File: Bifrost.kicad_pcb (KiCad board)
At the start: 4 copper layers, 68.6 x 53.3 mm, 59 parts, among them J1 OIP, U1 AD5932, U2 BGA2851, U3 AD8000, U4 BGA2851, U5 AD5932, X1 SPXO-50M

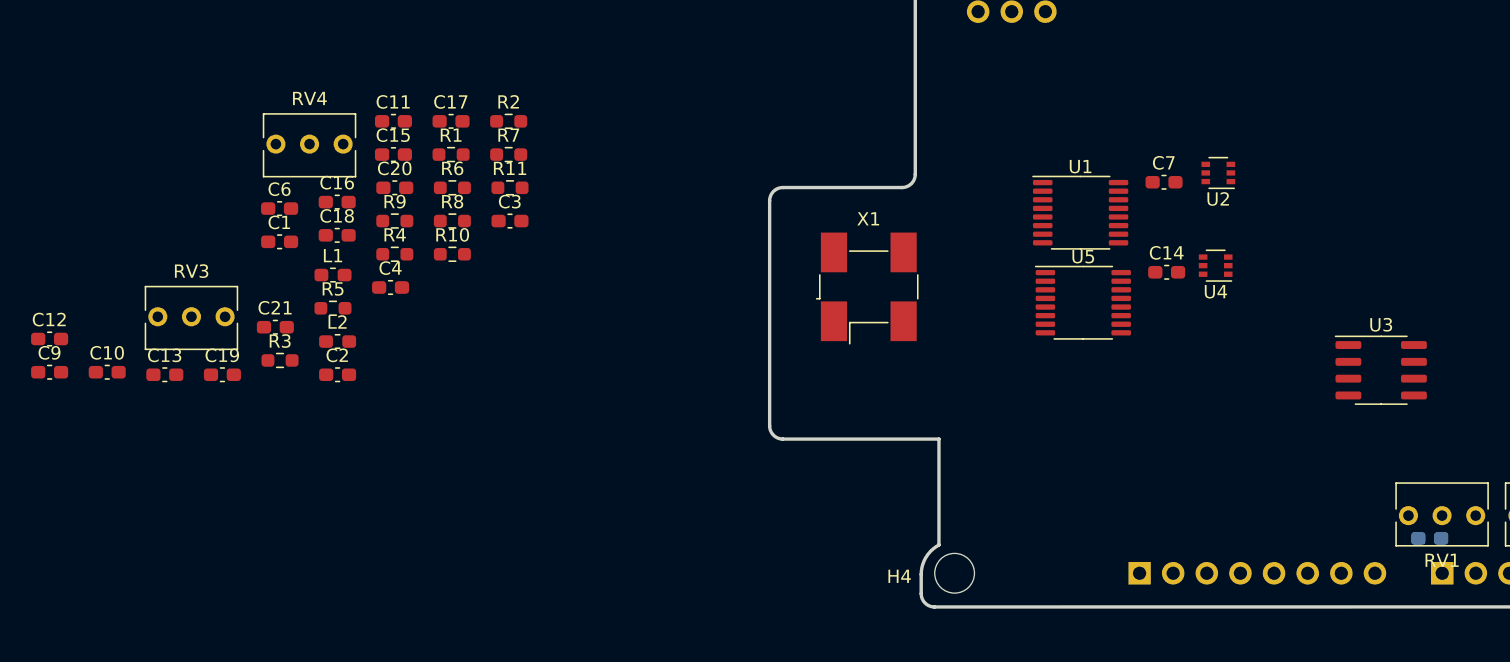
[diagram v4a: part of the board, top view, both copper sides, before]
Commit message: Progressed in placement
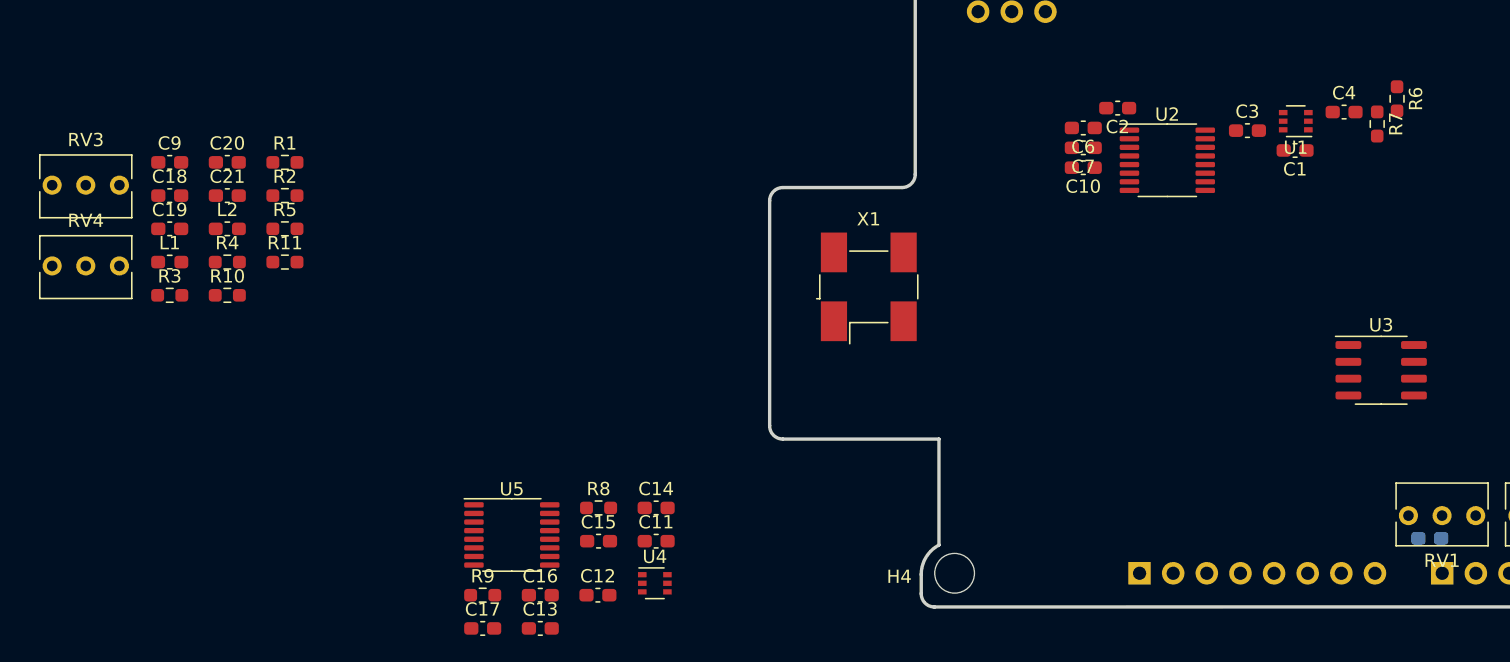
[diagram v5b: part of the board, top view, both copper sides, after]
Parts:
- C1: value 10n -> 100n
- C10, C15, C7: value 53n -> 100n
- C12, C2: value 100n -> 10n
- C13: value 10n -> 53n
- C3, C4: value 100n -> 53n
- U1: value AD5932 -> BGA2851; footprint Package_SO:TSSOP-16_4.4x5mm_P0.65mm -> Package_TO_SOT_SMD:SOT-363_SC-70-6
- U2: value BGA2851 -> AD5932; footprint Package_TO_SOT_SMD:SOT-363_SC-70-6 -> Package_SO:TSSOP-16_4.4x5mm_P0.65mm
- moved C1 77.0 mm to (153.9, 97.2), turned to 180 degrees
- moved C10 75.3 mm to (137.9, 98.5), turned to 180 degrees
- moved C4 73.2 mm to (157.6, 94.3)
- moved R6 71.7 mm to (161.6, 93.3), turned to 270 degrees
- moved R7 65.6 mm to (160.1, 95.2), turned to 270 degrees
- moved C2 62.3 mm to (140.5, 94.0), turned to 180 degrees
- moved C6 61.0 mm to (137.9, 95.5), turned to 180 degrees
- moved C3 56.1 mm to (150.3, 95.7)
- moved U4 48.7 mm to (105.5, 129.9), turned to 0 degrees
- moved U5 46.6 mm to (94.7, 126.2)
- moved C12 45.7 mm to (101.2, 130.8)
- moved C14 42.5 mm to (105.6, 124.2)
- moved C17 38.4 mm to (92.5, 133.3)
- moved C11 37.4 mm to (105.6, 126.7)
- moved C13 34.2 mm to (96.9, 133.3)
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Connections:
- AD1 pad 2: (no net) -> /AD1
- AD1 pad 3: (no net) -> /AD2
- AD1 pad 5: (no net) -> /AD4
- AD1 pad 6: (no net) -> /AD5
- C1 pad 1: Net-(C1-Pad1) -> VDDA
- C1 pad 2: VDDA -> GND
- C10 pad 2: Net-(C10-Pad2) -> GND
- C12 pad 1: VDDA -> Net-(C12-Pad1)
- C12 pad 2: GND -> VDDA
- C13 pad 2: VDDA -> Net-(C13-Pad2)
- C14 pad 2: Net-(C14-Pad2) -> /sheet61E7139B/Fout
- C15 pad 1: Net-(C15-Pad1) -> VDDA
- C15 pad 2: Net-(C15-Pad2) -> GND
- C16 pad 1: Net-(C16-Pad1) -> VDD
- C17 pad 1: VDD -> Net-(C17-Pad1)
- C2 pad 1: VDDA -> Net-(C2-Pad1)
- C2 pad 2: GND -> VDDA
- C3 pad 1: VDD -> Net-(C3-Pad1)
- C3 pad 2: GND -> Net-(C3-Pad2)
- C4 pad 2: GND -> /Sheet61C59086/Fout
- C7 pad 1: Net-(C7-Pad1) -> VDD
- C7 pad 2: Net-(C7-Pad2) -> GND
- ICSP1 pad 1: (no net) -> /MISO2
- ICSP1 pad 2: (no net) -> /+5V_Adr_3
- ICSP1 pad 3: (no net) -> /SCK2
- ICSP1 pad 4: (no net) -> /MOSI2
- ICSP1 pad 5: (no net) -> /RESET2
- ICSP2 pad 1: (no net) -> /MISO_0
- ICSP2 pad 3: (no net) -> /SCK_0
- ICSP2 pad 4: (no net) -> /MOSI_0
- ICSP2 pad 5: (no net) -> /RESET_0
- IOH1 pad 1: (no net) -> /IO8
- IOH1 pad 10: (no net) -> /SCL
- IOH1 pad 2: (no net) -> /IO9
- IOH1 pad 3: /SEN -> /SS
- IOH1 pad 8: (no net) -> /AREF
- IOH1 pad 9: (no net) -> /SDA
- IOL1 pad 1: (no net) -> /IO0
- IOL1 pad 2: (no net) -> /IO1
- POWER1 pad 1: (no net) -> Net-(POWER1-Pad1)
- POWER1 pad 3: (no net) -> /RESET
- POWER1 pad 4: (no net) -> /+3V3
- POWER1 pad 5: (no net) -> /+5V_Ard_1
- POWER1 pad 8: (no net) -> /VIN
- R2 pad 2: Net-(C10-Pad2) -> /Sheet61C59086/Fout
- R3 pad 2: Net-(C15-Pad2) -> /sheet61E7139B/Fout
- R49 pad 1: /SCK_S -> /SCK
- R52 pad 1: /SDI_S -> /MOSI
- R52 pad 2: /MOSI -> /SDI
- R53 pad 1: (no net) -> /IO9
- R53 pad 2: /MISO -> /SEN2
- R56 pad 1: /SEN_S -> /SS
- R6 pad 2: Net-(C10-Pad2) -> /Sheet61C59086/Fout
- R7 pad 1: Net-(C10-Pad2) -> /Sheet61C59086/Fout
- R8 pad 2: Net-(C15-Pad2) -> /sheet61E7139B/Fout
- R9 pad 1: Net-(C15-Pad2) -> /sheet61E7139B/Fout
- U1 pad 1: Net-(C1-Pad1) -> VDDA
- U1 pad 2: VDDA -> GND
- U1 pad 3: VDD -> Net-(C4-Pad1)
- U1 pad 4: Net-(C4-Pad1) -> GND
- U1 pad 6: Net-(U1-Pad6) -> Net-(C3-Pad2)
- U2 pad 1: VDDA -> Net-(C2-Pad1)
- U2 pad 2: GND -> VDDA
- U2 pad 3: Net-(C10-Pad1) -> VDD
- U2 pad 4: GND -> Net-(C10-Pad1)
- U2 pad 6: Net-(C7-Pad2) -> /Sheet61C59086/MCLK
- U3 pad 1: (no net) -> Net-(U3-Pad1)
- U3 pad 5: (no net) -> Net-(U3-Pad5)
- U3 pad 8: (no net) -> Net-(U3-Pad8)
- U4 pad 3: Net-(C15-Pad1) -> Net-(C14-Pad1)
- U4 pad 6: Net-(C14-Pad2) -> Net-(C13-Pad2)
- U5 pad 1: Net-(C13-Pad1) -> Net-(C12-Pad1)
- U5 pad 11: /SDI_S -> /SDI
- U5 pad 12: /SCK_S -> /SCK
- U5 pad 13: /SEN_S -> /SEN2
- U5 pad 16: Net-(C14-Pad1) -> Net-(C13-Pad1)
- U5 pad 4: Net-(C16-Pad1) -> Net-(C17-Pad1)
- U5 pad 6: Net-(U1-Pad6) -> /Sheet61C59086/MCLK
- U5 pad 7: (no net) -> Net-(U5-Pad7)
- U5 pad 8: (no net) -> Net-(U5-Pad8)
- X1 pad 1: (no net) -> Net-(X1-Pad1)
- X1 pad 3: Net-(U1-Pad6) -> /Sheet61C59086/MCLK

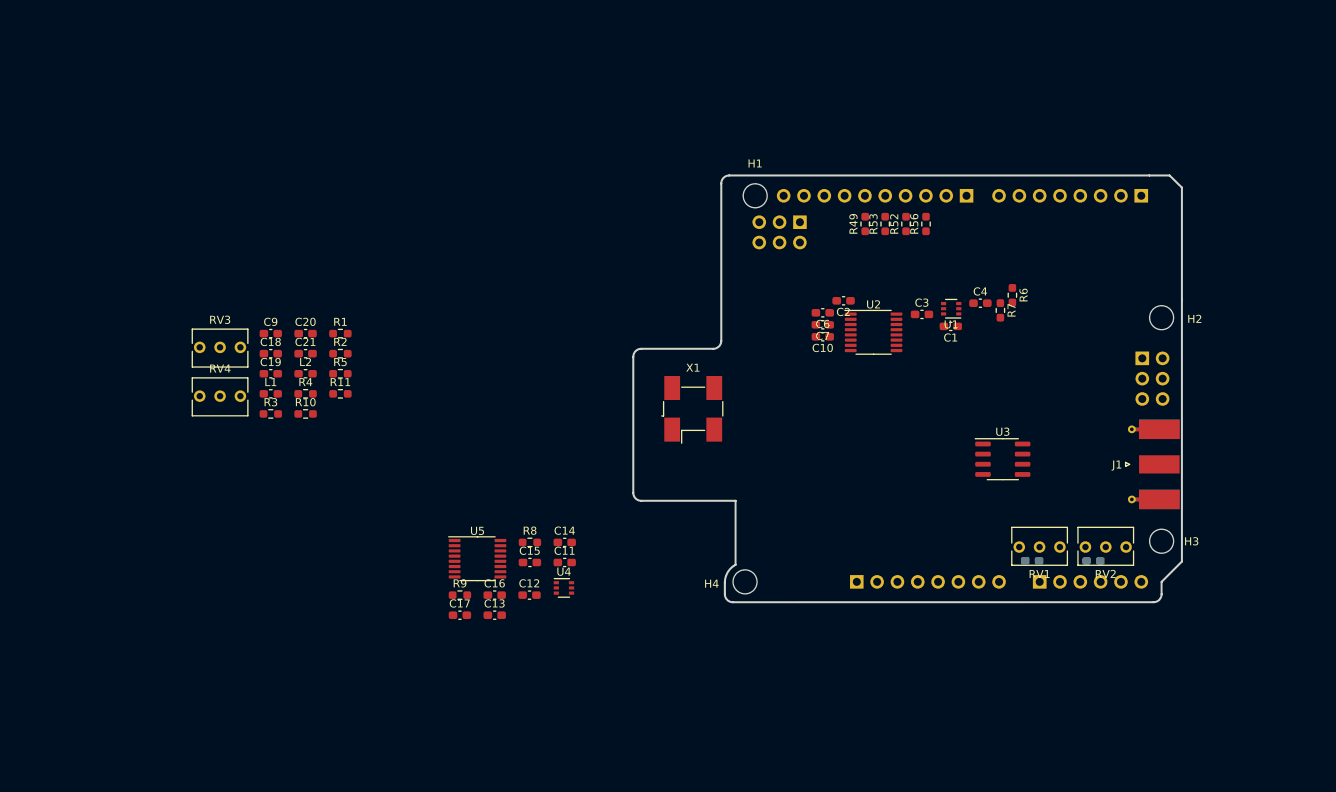
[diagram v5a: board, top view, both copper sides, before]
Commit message: Implemented the LMH6881 instead of the AD8000 Continued routing
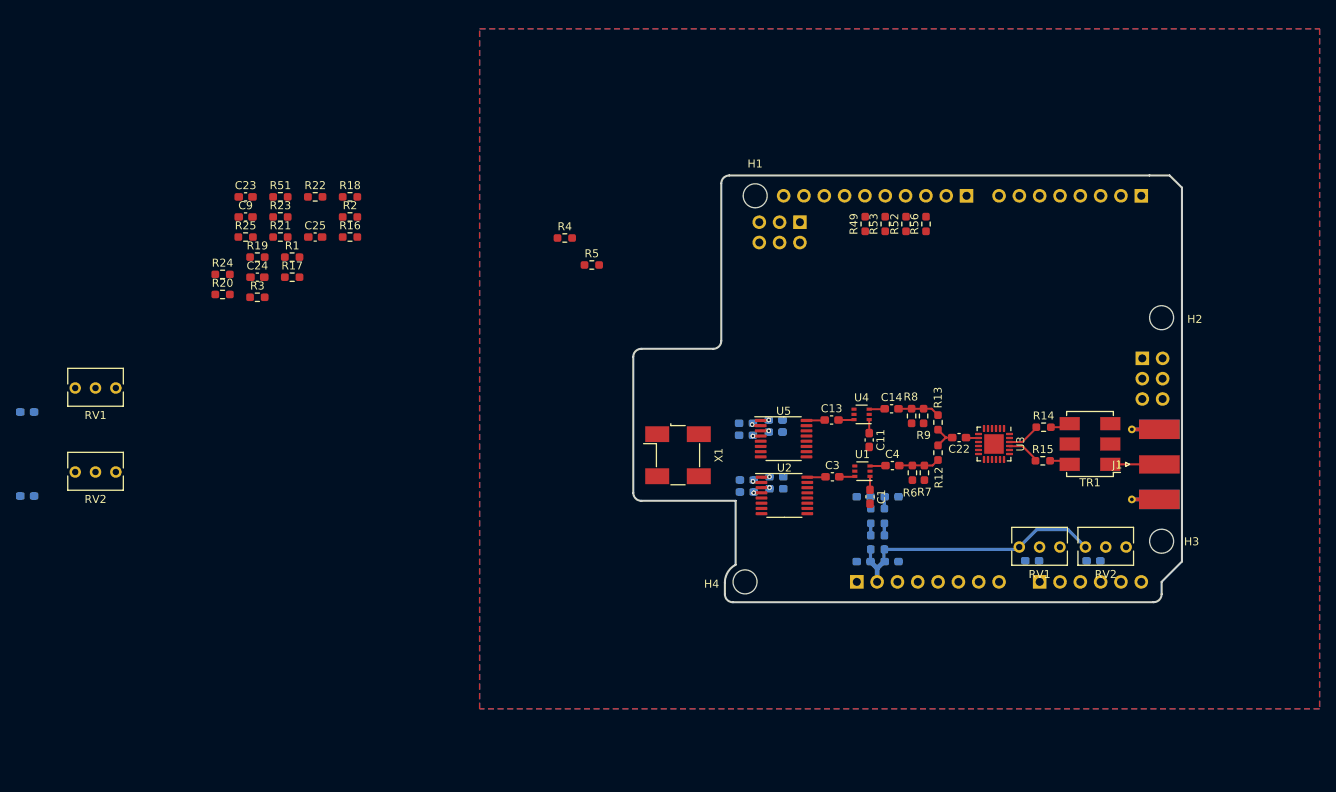
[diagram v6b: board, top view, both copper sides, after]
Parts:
- removed RV3, RV4: POT, Potentiometer_THT:Potentiometer_Bourns_3266Y_Vertical
- added C22: 10n, Capacitor_SMD:C_0603_1608Metric_Pad1.08x0.95mm_HandSolder, F.Cu at (154.9, 111.1)
- added C23: 1n, Capacitor_SMD:C_0603_1608Metric_Pad1.08x0.95mm_HandSolder, F.Cu at (65.8, 81.0)
- added C24: 10n, Capacitor_SMD:C_0603_1608Metric_Pad1.08x0.95mm_HandSolder, F.Cu at (67.2, 91.0)
- added C25: 10n, Capacitor_SMD:C_0603_1608Metric_Pad1.08x0.95mm_HandSolder, F.Cu at (74.5, 86.0)
- added C5: 100n, Capacitor_SMD:C_0603_1608Metric_Pad1.08x0.95mm_HandSolder, B.Cu at (38.5, 107.9)
- added C8: 100n, Capacitor_SMD:C_0603_1608Metric_Pad1.08x0.95mm_HandSolder, B.Cu at (38.5, 118.4)
- added R12: 50, Resistor_SMD:R_0603_1608Metric_Pad0.98x0.95mm_HandSolder, F.Cu at (152.3, 113.0)
- added R13: 50, Resistor_SMD:R_0603_1608Metric_Pad0.98x0.95mm_HandSolder, F.Cu at (152.3, 109.2)
- added R14: 50, Resistor_SMD:R_0603_1608Metric_Pad0.98x0.95mm_HandSolder, F.Cu at (165.5, 109.8)
- added R15: 50, Resistor_SMD:R_0603_1608Metric_Pad0.98x0.95mm_HandSolder, F.Cu at (165.4, 114.0)
- added R16: 50, Resistor_SMD:R_0603_1608Metric_Pad0.98x0.95mm_HandSolder, F.Cu at (78.8, 86.0)
- added R17: NP, Resistor_SMD:R_0603_1608Metric_Pad0.98x0.95mm_HandSolder, F.Cu at (71.6, 91.0)
- added R18: 0, Resistor_SMD:R_0603_1608Metric_Pad0.98x0.95mm_HandSolder, F.Cu at (78.8, 81.0)
- added R19: NP, Resistor_SMD:R_0603_1608Metric_Pad0.98x0.95mm_HandSolder, F.Cu at (67.2, 88.5)
- added R20: 0, Resistor_SMD:R_0603_1608Metric_Pad0.98x0.95mm_HandSolder, F.Cu at (62.9, 93.2)
- added R21: NP, Resistor_SMD:R_0603_1608Metric_Pad0.98x0.95mm_HandSolder, F.Cu at (70.1, 86.0)
- added R22: 0, Resistor_SMD:R_0603_1608Metric_Pad0.98x0.95mm_HandSolder, F.Cu at (74.5, 81.0)
- added R23: NP, Resistor_SMD:R_0603_1608Metric_Pad0.98x0.95mm_HandSolder, F.Cu at (70.1, 83.5)
- added R24: 0, Resistor_SMD:R_0603_1608Metric_Pad0.98x0.95mm_HandSolder, F.Cu at (62.9, 90.7)
- added R25: 300, Resistor_SMD:R_0603_1608Metric_Pad0.98x0.95mm_HandSolder, F.Cu at (65.8, 86.0)
- added R51: 300, Resistor_SMD:R_0603_1608Metric_Pad0.98x0.95mm_HandSolder, F.Cu at (70.1, 81.0)
- added RV1: POT_Mod_Freq1, Potentiometer_THT:Potentiometer_Bourns_3266Y_Vertical, F.Cu at (44.5, 104.9)
- added RV2: POT_Mod_Freq2, Potentiometer_THT:Potentiometer_Bourns_3266Y_Vertical, F.Cu at (44.5, 115.4)
- added TR1: ADT2-1T, RF_Mini-Circuits:Mini-Circuits_CD542_H2.84mm, F.Cu at (171.3, 111.9)
- C10, C12, C15, C16, C17, C18, C19, C2, C20, C21, C6, C7, L1, L2, R10, R11: moved to B.Cu
- C9: value 1u -> 10n
- R1: value 15k -> 1k
- R2: value 5k -> NP
- R3: value 5k -> 0
- R4: value 1k -> 2k
- U3: value AD8000 -> LMH6881; footprint Package_SO:SOIC-8_3.9x4.9mm_P1.27mm -> Package_DFN_QFN:WQFN-24-1EP_4x4mm_P0.5mm_EP2.45x2.45mm
- moved C20 78.6 mm to (146.5, 126.6), turned to 180 degrees
- moved C18 78.5 mm to (143.0, 126.6)
- moved L1 77.3 mm to (143.9, 124.2), turned to 90 degrees
- moved C19 75.7 mm to (143.0, 118.5)
- moved C21 75.4 mm to (146.5, 118.5), turned to 180 degrees
- moved L2 75.4 mm to (145.6, 124.2), turned to 90 degrees
- moved R10 71.8 mm to (143.9, 120.9), turned to 270 degrees
- moved R11 69.7 mm to (145.6, 120.9), turned to 270 degrees
- moved R9 62.1 mm to (150.5, 108.4), turned to 270 degrees
- moved R8 50.3 mm to (149.0, 108.4), turned to 90 degrees
- moved C13 48.7 mm to (139.0, 108.9)
- moved C14 44.1 mm to (146.5, 107.5)
- moved U4 43.1 mm to (142.8, 108.2), turned to 180 degrees
- moved C17 42.2 mm to (128.3, 110.8), turned to 180 degrees
- moved U5 41.1 mm to (133.0, 111.2)
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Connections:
- AD1 pad 2: /AD1 -> (no net)
- AD1 pad 3: /AD2 -> (no net)
- AD1 pad 5: /AD4 -> (no net)
- AD1 pad 6: /AD5 -> (no net)
- C1 pad 1: VDDA -> VCC
- C11 pad 1: VDDA -> VCC
- C12 pad 2: VDDA -> VCC
- C15 pad 1: VDDA -> VCC
- C18 pad 2: /+5V_Ard_0 -> /+5V_Ard_2
- C2 pad 2: VDDA -> VCC
- C20 pad 2: /+5V_Ard_0 -> /+5V_Ard_2
- C21 pad 2: VDDA -> VCC
- C6 pad 1: VDDA -> VCC
- C9 pad 1: Net-(C9-Pad1) -> GND
- C9 pad 2: Net-(C9-Pad2) -> VCC
- ICSP1 pad 1: /MISO2 -> (no net)
- ICSP1 pad 2: /+5V_Adr_3 -> (no net)
- ICSP1 pad 3: /SCK2 -> (no net)
- ICSP1 pad 4: /MOSI2 -> (no net)
- ICSP1 pad 5: /RESET2 -> (no net)
- ICSP2 pad 1: /MISO_0 -> (no net)
- ICSP2 pad 3: /SCK_0 -> (no net)
- ICSP2 pad 4: /MOSI_0 -> (no net)
- ICSP2 pad 5: /RESET_0 -> (no net)
- IOH1 pad 10: /SCL -> (no net)
- IOH1 pad 8: /AREF -> (no net)
- IOH1 pad 9: /SDA -> (no net)
- IOL1 pad 1: /IO0 -> (no net)
- IOL1 pad 2: /IO1 -> (no net)
- J1 pad 1: Net-(C9-Pad2) -> Net-(J1-Pad1)
- L1 pad 1: /+5V_Ard_0 -> /+5V_Ard_2
- L2 pad 1: /+5V_Ard_0 -> /+5V_Ard_2
- POWER1 pad 1: Net-(POWER1-Pad1) -> (no net)
- POWER1 pad 3: /RESET -> (no net)
- POWER1 pad 4: /+3V3 -> (no net)
- POWER1 pad 5: /+5V_Ard_1 -> (no net)
- POWER1 pad 8: /VIN -> (no net)
- R1 pad 1: Net-(C9-Pad1) -> /2.5V
- R1 pad 2: Net-(R1-Pad2) -> /1.25V
- R11 pad 1: VDDA -> VCC
- R2 pad 1: Net-(R2-Pad1) -> VCC
- R2 pad 2: /Sheet61C59086/Fout -> Net-(R2-Pad2)
- R3 pad 1: Net-(R3-Pad1) -> Net-(R2-Pad2)
- R3 pad 2: /sheet61E7139B/Fout -> GND
- R4 pad 1: +2V5 -> /2.5V
- R4 pad 2: VDDA -> VCC
- R5 pad 1: +2V5 -> /1.25V
- R6 pad 1: VDDA -> VCC
- R8 pad 1: VDDA -> VCC
- U1 pad 1: VDDA -> VCC
- U2 pad 14: /IO4 -> (no net)
- U2 pad 2: VDDA -> VCC
- U2 pad 7: Net-(U2-Pad7) -> (no net)
- U2 pad 8: Net-(U2-Pad8) -> (no net)
- U3 pad 2: Net-(R1-Pad2) -> /1.25V
- U3 pad 3: +2V5 -> Net-(R19-Pad1)
- U3 pad 4: GND -> Net-(R17-Pad1)
- U3 pad 5: Net-(U3-Pad5) -> Net-(R2-Pad2)
- U3 pad 6: Net-(C9-Pad1) -> GND
- U3 pad 7: /+5V_Ard_0 -> GND
- U4 pad 1: VDDA -> VCC
- U5 pad 14: /IO7 -> (no net)
- U5 pad 2: VDDA -> VCC
- U5 pad 7: Net-(U5-Pad7) -> (no net)
- U5 pad 8: Net-(U5-Pad8) -> (no net)
- X1 pad 1: Net-(X1-Pad1) -> (no net)
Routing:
- net /+5V_Ard_2: track 0.00 -> 34.2 mm
- net VCC: track 0.00 -> 7.11 mm, vias 0 -> 2
- net Net-(J1-Pad1): track 0.00 -> 6.13 mm
- net /sheet61E7139B/Fout: track 0.00 -> 5.27 mm
- net /Sheet61C59086/Fout: track 0.00 -> 5.13 mm
- net Net-(R15-Pad1): track 0.00 -> 4.15 mm
- net Net-(R14-Pad1): track 0.00 -> 4.07 mm
- net Net-(C22-Pad2): track 0.00 -> 3.58 mm
- net VDD: track 0.00 -> 3.49 mm, vias 0 -> 2
- net Net-(R15-Pad2): track 0.00 -> 2.63 mm
- net Net-(R14-Pad2): track 0.00 -> 2.53 mm
- net Net-(C3-Pad1): track 0.00 -> 2.30 mm
- net Net-(C13-Pad1): track 0.00 -> 2.30 mm
- net Net-(C4-Pad1): track 0.00 -> 1.96 mm
- net Net-(C13-Pad2): track 0.00 -> 1.96 mm
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- added copper zone on B.Cu, net GND
- added copper zone on F.Cu, net GND
- added copper zone on In1.Cu, net GND
- added copper zone on In2.Cu, net GND
